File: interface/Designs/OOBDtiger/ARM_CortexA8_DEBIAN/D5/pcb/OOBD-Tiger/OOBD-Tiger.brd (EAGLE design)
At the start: 63.4 x 38.2 mm, 122 parts, among them IC1 ADM3053M, IC2 ADM3053M, IC4 DS3231, U1 SY6280, U10 MP1482DS, U2 SN65HVD230(SO8), U3 SY6280, U6 SN65HVD230(SO8)

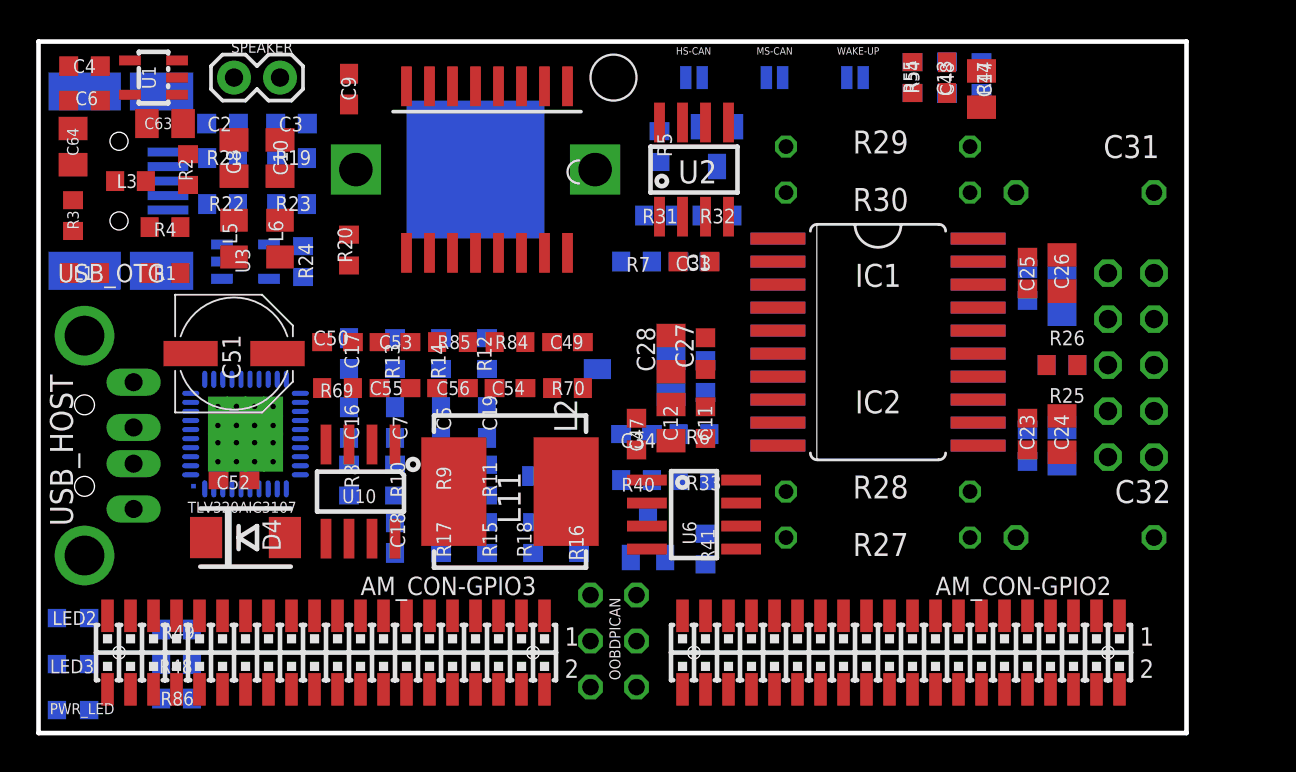
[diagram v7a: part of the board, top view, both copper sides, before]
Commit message: Funktionsgruppen Powersupply & Audio endplaziert
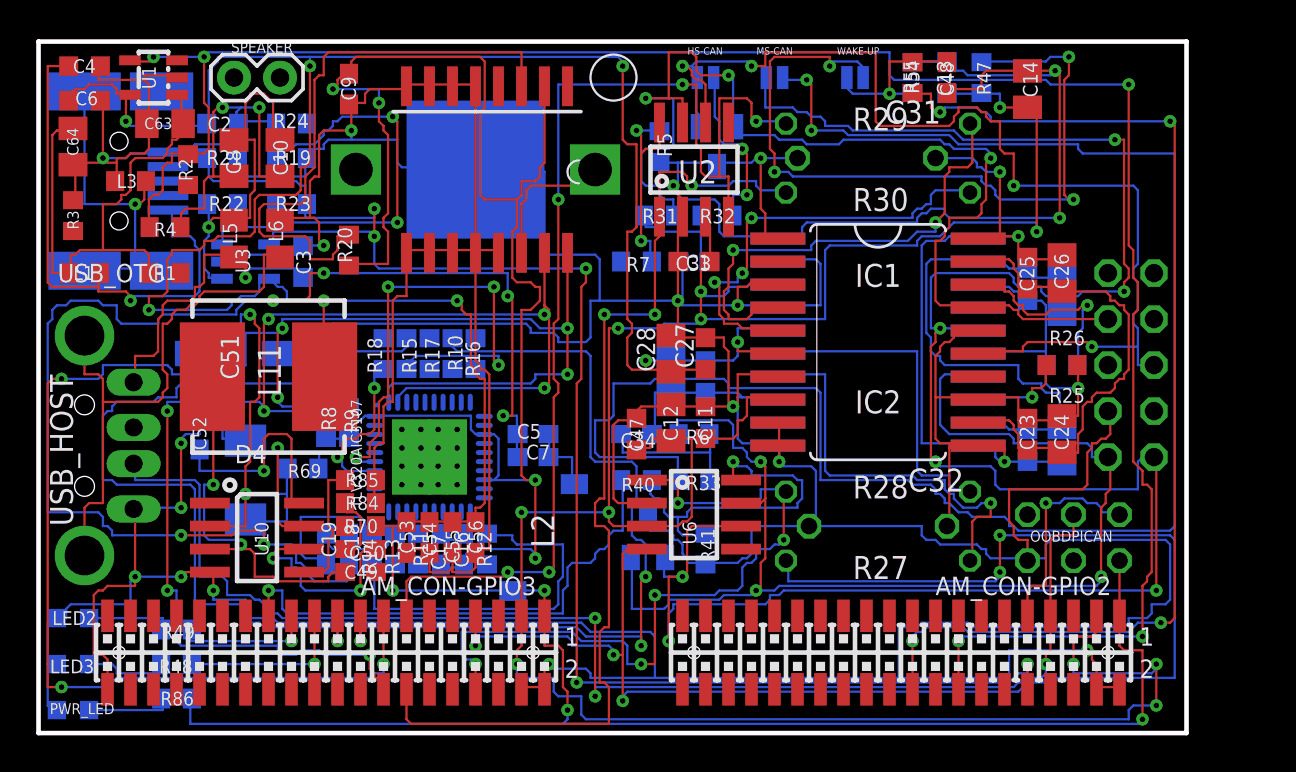
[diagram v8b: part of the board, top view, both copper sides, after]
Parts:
- moved OOBDPICAN 26.0 mm to (57.1, 10.8), turned to 0 degrees
- moved C49 17.1 mm to (17.8, 8.89), turned to 180 degrees
- moved L11 14.8 mm to (12.7, 19.7), turned to 0 degrees
- moved R70 13.7 mm to (17.8, 11.4)
- moved R18 13.1 mm to (19.1, 21.0)
- moved C31 12.2 mm to (45.7, 31.8)
- moved R84 12.1 mm to (17.8, 12.7)
- moved C17 11.9 mm to (22.2, 10.2), turned to 90 degrees
- moved R16 11.7 mm to (24.1, 21.0)
- moved C50 11.5 mm to (17.8, 10.2), turned to 180 degrees
- moved C32 11.4 mm to (46.4, 11.4)
- moved R14 11.4 mm to (18.4, 10.2)
- moved C19 11.3 mm to (15.9, 10.2)
- moved R15 11.1 mm to (20.3, 21.0)
- moved C53 10.8 mm to (20.3, 10.8), turned to 270 degrees
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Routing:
- net GND: track 0.00 -> 509.0 mm, vias 0 -> 20
- net +5V: track 0.00 -> 220.4 mm, vias 0 -> 12
- net 3V3: track 0.00 -> 145.9 mm, vias 0 -> 11
- net CAN0_L: track 0.00 -> 119.5 mm, vias 0 -> 7
- net USB0_DRV: track 0.00 -> 113.8 mm, vias 0 -> 5
- net I2C0-SCL: track 0.00 -> 96.4 mm, vias 0 -> 7
- net N$32: track 0.00 -> 94.4 mm, vias 0 -> 2
- net +3V3: track 0.00 -> 86.9 mm, vias 0 -> 4
- net GNDA: track 0.00 -> 86.2 mm, vias 0 -> 4
- net DCAN0_RX: track 0.00 -> 84.4 mm, vias 0 -> 5
- net USB1_DRV: track 0.00 -> 84.2 mm, vias 0 -> 5
- net I2C0-SDA: track 0.00 -> 75.9 mm, vias 0 -> 7
- net AGND: track 0.00 -> 74.8 mm, vias 0 -> 6
- net USB1_DP: track 0.00 -> 73.1 mm, vias 0 -> 3
- net CAN0_H: track 0.00 -> 68.1 mm, vias 0 -> 3
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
